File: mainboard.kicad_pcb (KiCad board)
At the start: 2 copper layers, 81.3 x 73 mm, 63 parts, among them J1 Screw_Terminal_1x02, J2 SERVO 5V, Q1 IRLR024NPBF, U1 AT90CAN128-16MU, U2 MCP2551-I/SN, U3 EP_MODULE, Y1 Crystal

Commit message: Small modif
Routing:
- net +5V: track 308.3 -> 307.7 mm
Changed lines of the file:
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@@
   (general
     (links 227)
-    (no_connects 7)
+    (no_connects 6)
     (area 62.154999 36.246999 143.585001 109.422001)
     (thickness 1.6)
-    (drawings 237)
-    (tracks 734)
+    (drawings 238)
+    (tracks 732)
     (zones 0)
     (modules 63)
@@
     (pad 1 thru_hole circle (at 0 0) (size 4.064 4.064) (drill 3.048) (layers *.Cu *.Mask F.SilkS))
   )
+  (gr_line (start 122.0216 92.1512) (end 120.3452 90.4748) (angle 90) (layer B.Paste) (width 0.2))
   (gr_line (start 108.331 57.277) (end 76.581 57.277) (angle 90) (layer B.Paste) (width 0.2))
   (gr_line (start 108.331 53.467) (end 108.331 57.277) (angle 90) (layer B.Paste) (width 0.2))
@@
   (gr_line (start 70.8025 86.487) (end 70.8025 106.934) (angle 90) (layer B.Paste) (width 0.2))
   (gr_line (start 62.738 86.487) (end 70.8025 86.487) (angle 90) (layer B.Paste) (width 0.2))
-  (gr_text PC (at 120.396 92.456) (layer B.Paste)
+  (gr_text PC (at 120.142 89.408) (layer B.Paste)
     (effects (font (size 1.5 1.5) (thickness 0.3)) (justify mirror))
   )
@@
   (segment (start 101.962 80.3465) (end 104.5465 82.931) (width 0.5) (layer F.Cu) (net 3))
   (segment (start 104.5465 82.931) (end 105.723 82.931) (width 0.5) (layer F.Cu) (net 3))
+  (segment (start 125.984 55.278) (end 125.984 57.3024) (width 0.5) (layer F.Cu) (net 4) (status 400000))
+  (segment (start 125.984 57.3024) (end 125.6284 57.658) (width 0.5) (layer F.Cu) (net 4))
+  (segment (start 123.8145 57.658) (end 125.6284 57.658) (width 0.5) (layer F.Cu) (net 4) (status 400000))
+  (segment (start 125.6284 57.658) (end 126.8835 57.658) (width 0.5) (layer F.Cu) (net 4) (status 800000))
   (segment (start 108.9152 61.5456) (end 122.452 61.5456) (width 0.5) (layer F.Cu) (net 4) (status 400000))
   (segment (start 123.8145 60.1831) (end 123.8145 57.658) (width 0.5) (layer F.Cu) (net 4) (status 800000))
   (segment (start 122.452 61.5456) (end 123.8145 60.1831) (width 0.5) (layer F.Cu) (net 4))
-  (segment (start 123.8145 57.658) (end 124.4092 57.658) (width 0.5) (layer F.Cu) (net 4))
-  (segment (start 126.8835 57.658) (end 124.4092 57.658) (width 0.5) (layer F.Cu) (net 4))
-  (segment (start 124.4092 57.658) (end 124.2568 57.8104) (width 0.5) (layer F.Cu) (net 4))
-  (segment (start 124.2568 57.8104) (end 123.8145 57.658) (width 0.5) (layer F.Cu) (net 4))
   (segment (start 99.562 78.82) (end 99.562 76.5242) (width 0.5) (layer F.Cu) (net 4))
   (segment (start 95.504 60.7441) (end 95.504 55.499) (width 0.5) (layer B.Cu) (net 4))
@@
   (segment (start 119.5832 45.5422) (end 120.2944 44.831) (width 0.5) (layer F.Cu) (net 4))
   (segment (start 120.2944 44.831) (end 121.666 44.831) (width 0.5) (layer F.Cu) (net 4))
-  (segment (start 126.1342 57.658) (end 126.1342 55.4282) (width 0.5) (layer F.Cu) (net 4))
-  (segment (start 126.1342 55.4282) (end 125.984 55.278) (width 0.5) (layer F.Cu) (net 4))
   (segment (start 95.274 61.087) (end 95.274 56.699) (width 0.5) (layer F.Cu) (net 4))
   (segment (start 95.274 56.699) (end 94.074 55.499) (width 0.5) (layer F.Cu) (net 4))

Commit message: Small modifs, but important
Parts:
- removed the REF** at (139.7, 40.1)
- removed the REF** at (139.7, 105.5)
- removed eREF**: 1pin, Connect:1pin
- added REF**: 1pin, Connect:1pin, F.Cu at (139.7, 40.1)
- added REF**: 1pin, Connect:1pin, F.Cu at (66.0, 40.1)
- added REF**: 1pin, Connect:1pin, F.Cu at (139.7, 105.5)
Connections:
- D1 pad 1: (no net) -> GND
- D1 pad 2: (no net) -> Net-(D1-Pad2)
- R7 pad 2: (no net) -> Net-(D1-Pad2)
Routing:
- net +5V: track 307.7 -> 334.1 mm
- net GND: track 164.1 -> 178.7 mm, vias 5 -> 7
- net PE1: track 37.0 -> 46.5 mm
- net Net-(D1-Pad2): track 0.00 -> 1.73 mm

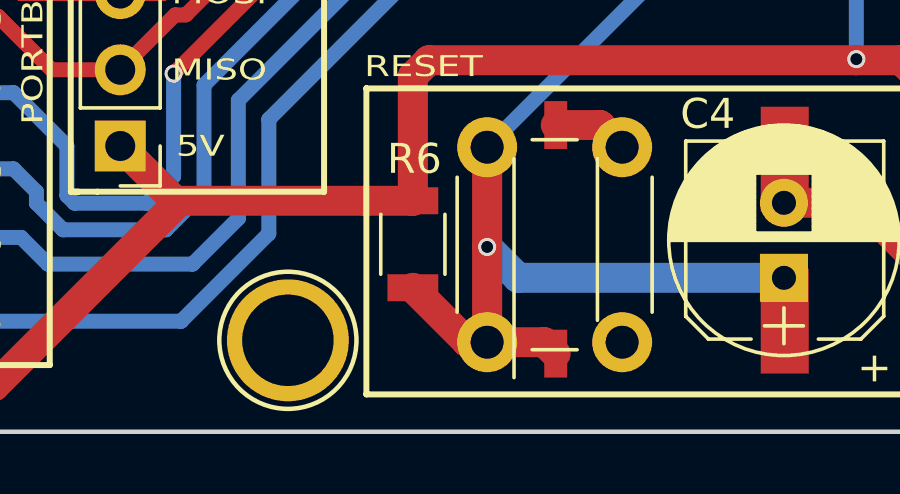
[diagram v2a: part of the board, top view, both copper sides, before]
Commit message: Changed some footprints from 0603 t 0805
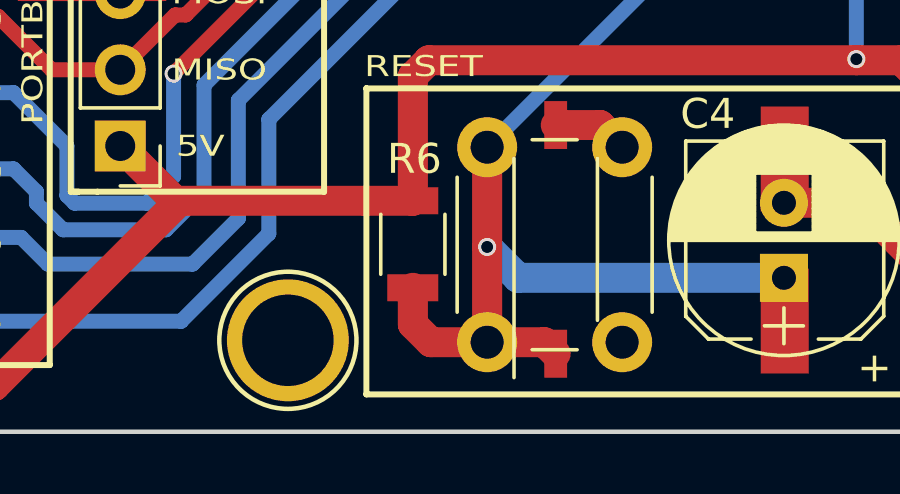
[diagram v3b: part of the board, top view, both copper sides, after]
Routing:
- net RESET: track 101.7 -> 102.4 mm
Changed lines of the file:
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@@
     (thickness 1.6)
     (drawings 238)
-    (tracks 758)
+    (tracks 759)
     (zones 0)
     (modules 63)
@@
   (segment (start 132.461 104.902) (end 132.461 98.8695) (width 1) (layer F.Cu) (net 4))
   (segment (start 132.461 98.8695) (end 133.5405 97.79) (width 1) (layer F.Cu) (net 4))
+  (segment (start 88.1761 106.3625) (end 86.2965 106.3625) (width 1) (layer F.Cu) (net 5) (status 400000))
+  (segment (start 85.6996 105.7656) (end 85.6996 104.5486) (width 1) (layer F.Cu) (net 5) (status 800000))
+  (segment (start 86.2965 106.3625) (end 85.6996 105.7656) (width 1) (layer F.Cu) (net 5))
   (segment (start 74.5236 38.9636) (end 74.5236 51.0286) (width 0.5) (layer B.Cu) (net 5))
   (segment (start 98.762 76.244) (end 98.762 78.82) (width 0.5) (layer F.Cu) (net 5))
@@
   (segment (start 88.1761 106.3625) (end 90.0811 106.3625) (width 1) (layer F.Cu) (net 5))
   (segment (start 90.0811 106.3625) (end 90.4621 106.7435) (width 1) (layer F.Cu) (net 5))
-  (segment (start 88.1761 106.3625) (end 87.5135 106.3625) (width 1) (layer F.Cu) (net 5))
-  (segment (start 87.5135 106.3625) (end 85.6996 104.5486) (width 1) (layer F.Cu) (net 5))
   (segment (start 124.026 47.498) (end 124.026 45.011) (width 0.5) (layer F.Cu) (net 6))
   (segment (start 124.026 45.011) (end 124.206 44.831) (width 0.5) (layer F.Cu) (net 6))
